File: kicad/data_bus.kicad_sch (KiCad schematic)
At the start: 15 parts, among them U18 SN74F377AN, U26 SN74F541N, U27 SN74F541N

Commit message: Tidy every schematic sheet: spread parts, straight runs, buses kept, horizontal tabs
Shared port, expansion and cartridge sheets laid out by hand; buses from
other sheets get a bus label at each chip, busy control nets a label at
each pin; some PLD and connector symbols reordered so wires run straight;
sideways power symbols read across. 0 netlist problems, no overlaps.

Co-Authored-By: Claude Opus 5.5 (1M context) <noreply@anthropic.com>
Claude-Session: https://claude.ai/code/session_01L9AkLuEg13EebxDmgXsaEp
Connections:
- net D0: now also R601.1; no longer R601.2
- net D1: now also R602.1; no longer R602.2
- net D2: now also R603.1; no longer R603.2
- net D3: now also R604.1; no longer R604.2
- net D4: now also R605.1; no longer R605.2
- net D5: now also R606.1; no longer R606.2
- net D6: now also R607.1; no longer R607.2
- net D7: now also R608.1; no longer R608.2
- net SRC0: now also R601.2; no longer R601.1
- net SRC1: now also R602.2; no longer R602.1
- net SRC2: now also R603.2; no longer R603.1
- net SRC3: now also R604.2; no longer R604.1
- net SRC4: now also R605.2; no longer R605.1
- net SRC5: now also R606.2; no longer R606.1
- net SRC6: now also R607.2; no longer R607.1
- net SRC7: now also R608.2; no longer R608.1
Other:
- moved on the sheet: C18, C26, C27, U18, U26, U27

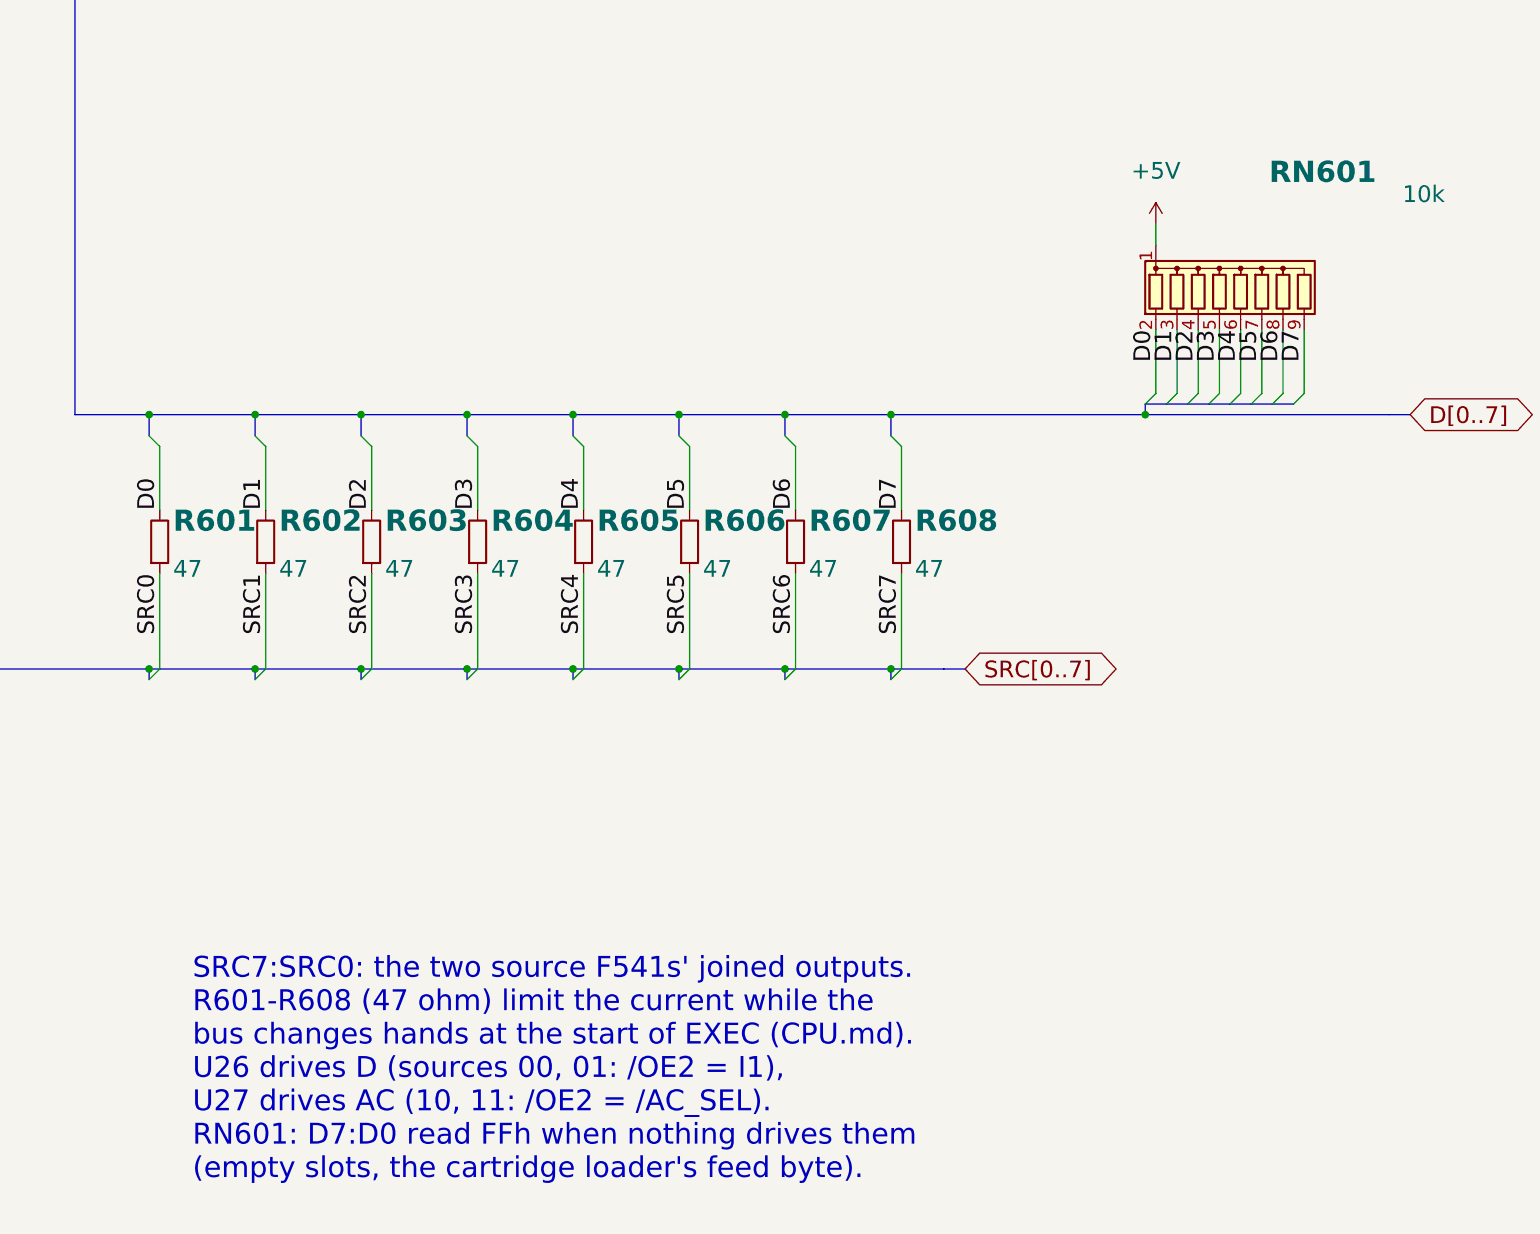
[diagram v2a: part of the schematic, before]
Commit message: Number parts from 1 for each kind; US zigzag resistor symbols
Main board R1-R54, RN1-RN2, D1-D5, JP1-JP2, F1, NT1, non-decoupling
capacitors C41-C46 (decaps keep Cn = Un); keyboard keys 1-63 row by row
(SWn, Dn, Rn per key). Resistors use R_US / R_Network08_US. --check now
fails on gaps or hundreds in the numbering. PDFs regenerated.

Co-Authored-By: Claude Opus 5.5 (1M context) <noreply@anthropic.com>
Claude-Session: https://claude.ai/code/session_01L9AkLuEg13EebxDmgXsaEp
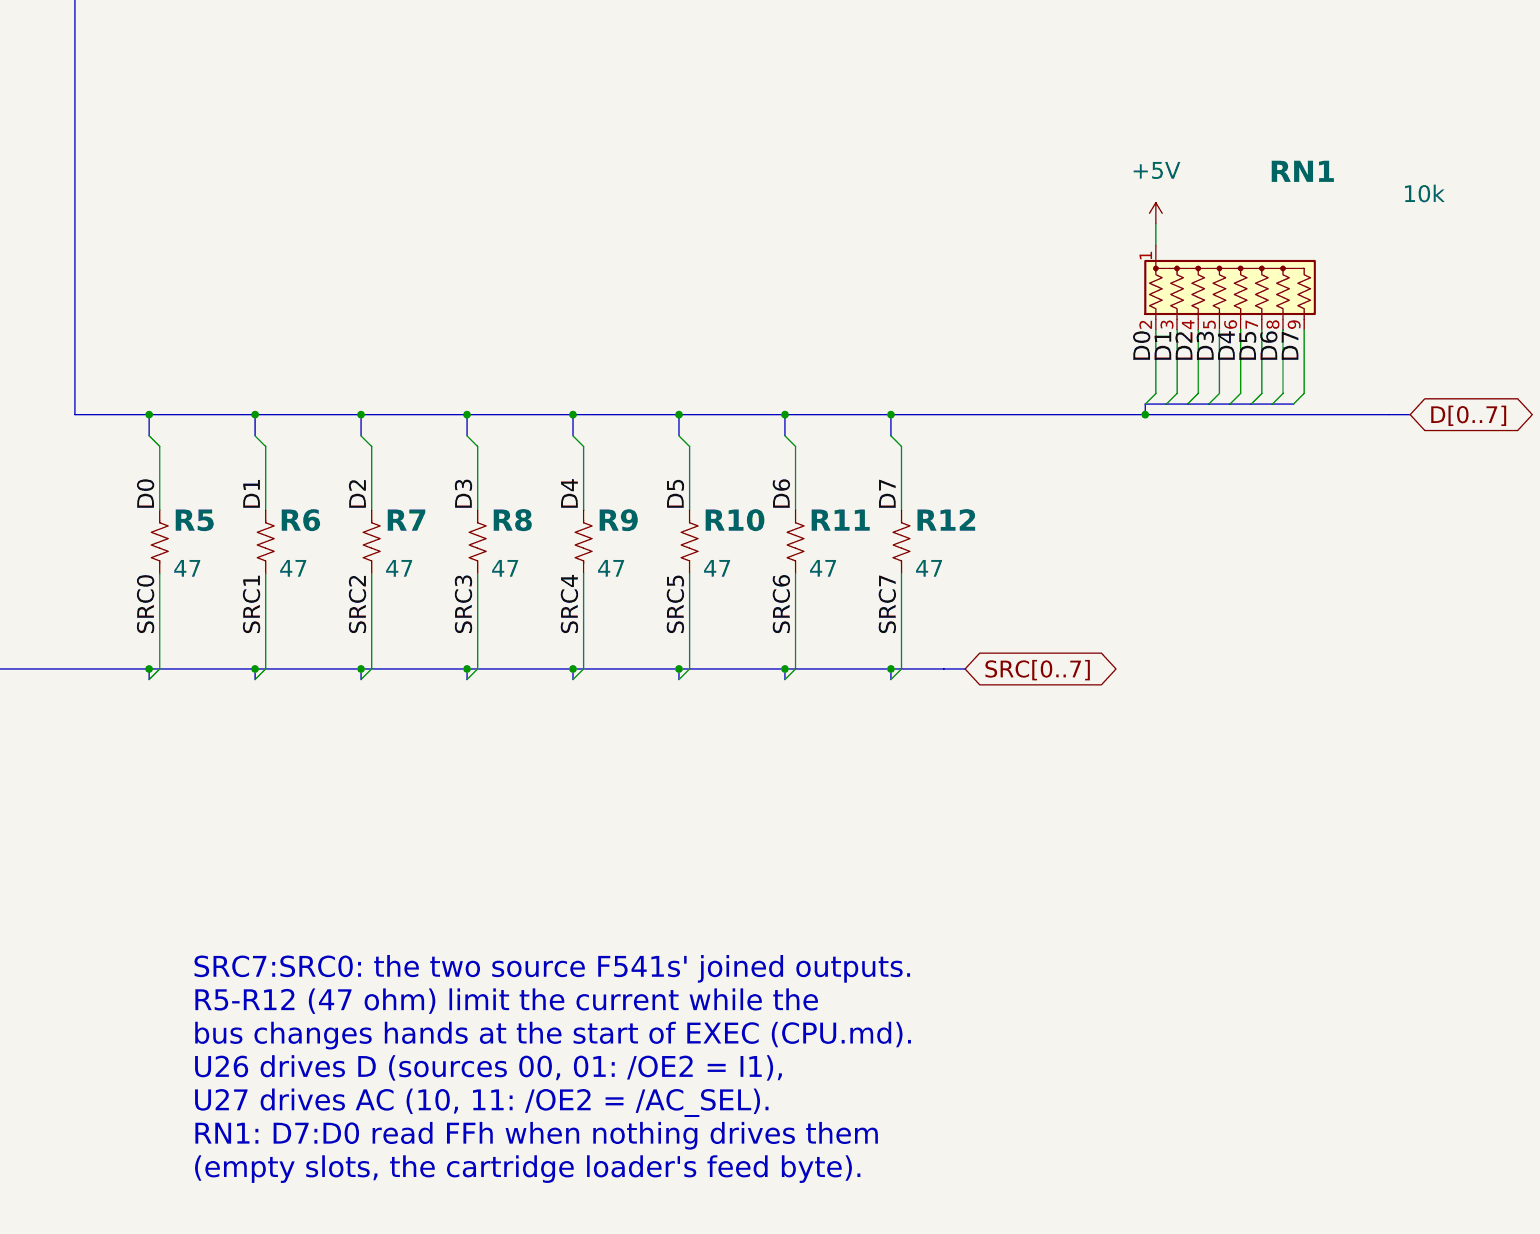
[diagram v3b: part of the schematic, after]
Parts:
- removed R601, R602, R603, R604, R605, R606, R607, R608: 47, Resistor_THT:R_Axial_DIN0207_L6.3mm_D2.5mm_P10.16mm_Horizontal, symbol placard_std:R
- removed RN601: 10k, Resistor_THT:R_Array_SIP9, symbol placard_std:R_Network08
- added R10, R11, R12, R5, R6, R7, R8, R9: 47, Resistor_THT:R_Axial_DIN0207_L6.3mm_D2.5mm_P10.16mm_Horizontal, symbol placard_std:R_US
- added RN1: 10k, Resistor_THT:R_Array_SIP9, symbol placard_std:R_Network08_US
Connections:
- net +5V: now also RN1.1 (common)
- net D0: now also R5.1, RN1.2 (R1)
- net D1: now also R6.1, RN1.3 (R2)
- net D2: now also R7.1, RN1.4 (R3)
- net D3: now also R8.1, RN1.5 (R4)
- net D4: now also R9.1, RN1.6 (R5)
- net D5: now also R10.1, RN1.7 (R6)
- net D6: now also R11.1, RN1.8 (R7)
- net D7: now also R12.1, RN1.9 (R8)
- net SRC0: now also R5.2
- net SRC1: now also R6.2
- net SRC2: now also R7.2
- net SRC3: now also R8.2
- net SRC4: now also R9.2
- net SRC5: now also R10.2
- net SRC6: now also R11.2
- net SRC7: now also R12.2
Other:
- note added: "R5-R12 (47 ohm) limit the current while the"
- note added: "RN1: D7:D0 read FFh when nothing drives them"
- note removed: "R601-R608 (47 ohm) limit the current while the"
- note removed: "RN601: D7:D0 read FFh when nothing drives them"

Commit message: Bill of materials for the main board, cartridge and keyboard
Manufacturer and MPN fields on every schematic part (empty where none is
chosen), set from an MPN table in gen_kicad_schematic.py; net tie, cartridge
edge fingers and solder jumper excluded from the BOM.  gen_bom.py groups the
parts by part number into docs/BOM.md and docs/BOM.csv, adding sockets,
shunts, keyboard LEDs, keycaps, stabilizers and the keyboard ribbon cable.

Co-Authored-By: Claude Opus 5.5 (1M context) <noreply@anthropic.com>
Claude-Session: https://claude.ai/code/session_018iEnPngycbxX6Tt4Wzp3zN
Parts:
- U18: MPN (none) -> SN74F377AN; Manufacturer (none) -> Texas Instruments
- U26, U27: MPN (none) -> SN74F541N; Manufacturer (none) -> Texas Instruments

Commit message: Part numbers for the remaining parts; J6 Tensility 54-00174; optional J1 and J9-J12
Every schematic part gets Manufacturer/MPN: Yageo MFR-25 resistors by value,
Bourns 4609X networks, KEMET/TDK ceramics, Panasonic FR electrolytics, ECS
oscillator, Assmann VGA, Sullins headers, Wurth box header, Cherry switches.
Sockets get On Shore numbers (0.3" 24/28-pin are ED241DT/ED281DT; ED28DT is
0.6"). J6 becomes the Tensility 54-00174 TRRS jack with a footprint drawn
from its datasheet. Digi-Key prices from Justin for the oscillator, VGA and
audio jack. The expansion slot sockets and the keyboard header are optional,
with a BOM total without them.

Co-Authored-By: Claude Opus 5.5 (1M context) <noreply@anthropic.com>
Claude-Session: https://claude.ai/code/session_01L9AkLuEg13EebxDmgXsaEp
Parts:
- C18, C26, C27: MPN (none) -> C320C104K5R5TA; Manufacturer (none) -> KEMET
- R10, R11, R12, R5, R6, R7, R8, R9: MPN (none) -> MFR-25FBF52-47R; Manufacturer (none) -> Yageo
- RN1: MPN (none) -> 4609X-101-103LF; Manufacturer (none) -> Bourns

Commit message: Kit footprints: DIP sockets with puller room and part number, resistors with value
Justin: put the chip-puller room in the socket footprints (User.Eco1,
2.5 mm past each end) and the part number in silkscreen between the pin
rows; resistors get their value in silkscreen on the body. New
gen_kicad_kit_footprints.py derives them from KiCad's stock footprints;
schematic, symbols, BOM and PDFs now name them. The board file is left
as is (Justin is editing it): Update PCB from Schematic swaps them in.

Co-Authored-By: Claude Opus 5.5 (1M context) <noreply@anthropic.com>
Claude-Session: https://claude.ai/code/session_01JnVuvUvdWezUUU6Sgmg16H
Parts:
- R10, R11, R12, R5, R6, R7, R8, R9: footprint Resistor_THT:R_Axial_DIN0207_L6.3mm_D2.5mm_P10.16mm_Horizontal -> placard:R_Axial_DIN0207_L6.3mm_D2.5mm_P10.16mm_Horizontal_Value
- U18, U26, U27: footprint Package_DIP:DIP-20_W7.62mm -> placard:DIP-20_W7.62mm_Socket_Puller
